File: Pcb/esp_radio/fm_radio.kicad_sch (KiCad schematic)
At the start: 21 parts, among them J3 Antenna, U5 RDA5807FP, Y2 32.768kHz

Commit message: Move custom components to kicad_common_library.
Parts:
- U5: symbol RDA5807FP:RDA5807FP -> kicad_common_lib:RDA5807FP
- renumbered TP10 to TP16, TP12 to TP17, TP11 to TP18
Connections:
- net +12V renamed +10V
- net I2C.SCLK renamed I2C.SCL
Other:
- note added: "Addr: 0b00100000"

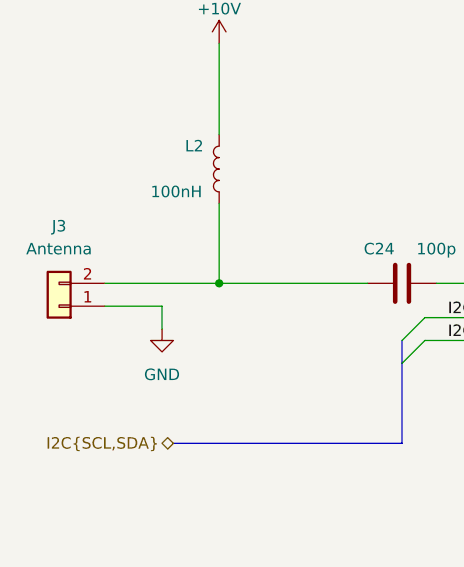
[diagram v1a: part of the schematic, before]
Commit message: Add components layout on PCB
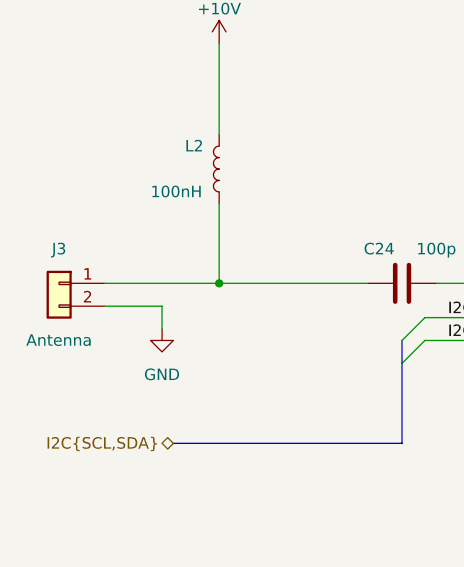
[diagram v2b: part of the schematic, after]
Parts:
- C24: footprint (none) -> kicad_common_lib:C_0805
- J3: footprint (none) -> Connector_JST:JST_XH_S2B-XH-A-1_1x02_P2.50mm_Horizontal
- L1, L2: footprint (none) -> Inductor_SMD:L_1206_3216Metric_Pad1.42x1.75mm_HandSolder
- R6: footprint (none) -> kicad_common_lib:R_0805
- TP16, TP17, TP18: footprint (none) -> TestPoint:TestPoint_THTPad_D2.0mm_Drill1.0mm
- Y2: footprint (none) -> Crystal:Crystal_HC18-U_Vertical
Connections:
- net GND: now also J3.2 (Pin_2); no longer J3.1 (Pin_1)
- net at C24.1, L2.1: now also J3.1 (Pin_1); no longer J3.2 (Pin_2)
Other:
- moved on the sheet: J3

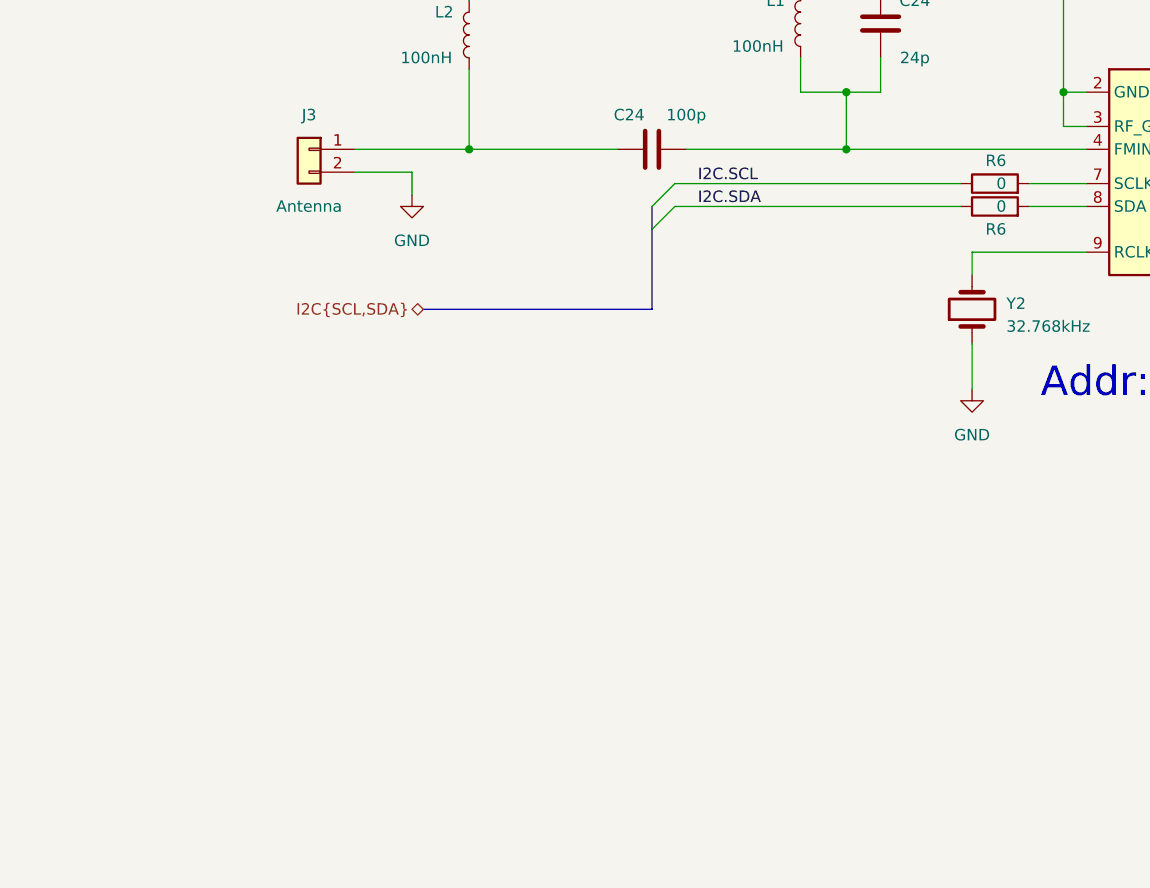
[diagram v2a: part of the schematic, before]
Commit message: Add chip select emulation for i2c devices
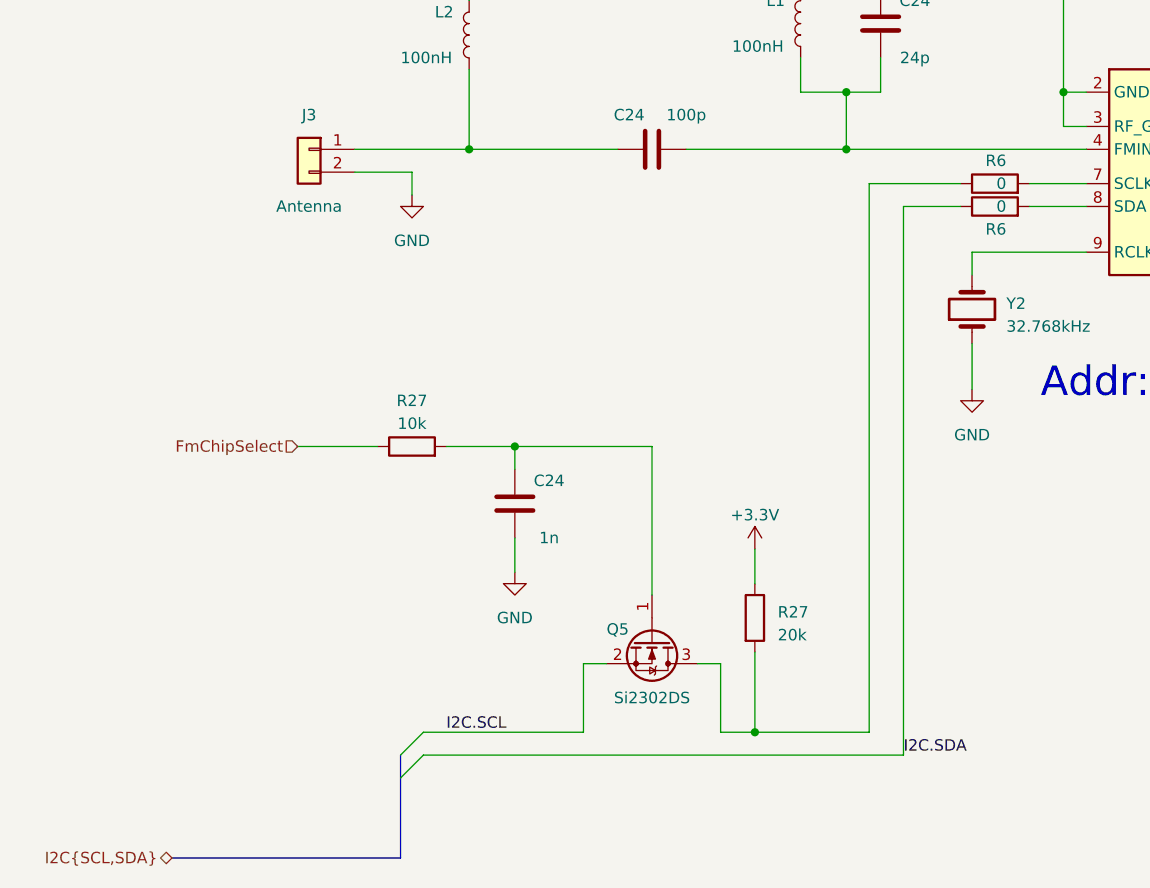
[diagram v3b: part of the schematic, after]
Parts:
- added C24: 1n, kicad_common_lib:C_0805, symbol Device:C
- added Q5: Si2302DS, Package_TO_SOT_SMD:SOT-23, symbol kicad_common_lib:AO3416
- added R27: 20k, kicad_common_lib:R_0805, symbol Device:R
- added R27: 10k, kicad_common_lib:R_0805, symbol Device:R
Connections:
- net +3.3V: now also R27.1
- net GND: now also C24.2
- net I2C.SCL: now also Q5.2 (S); no longer R6.1
- new net: C24.1, Q5.1 (G), R27.2
- new net: Q5.3 (D), R27.2, R6.1
- new net FmChipSelect: R27.1

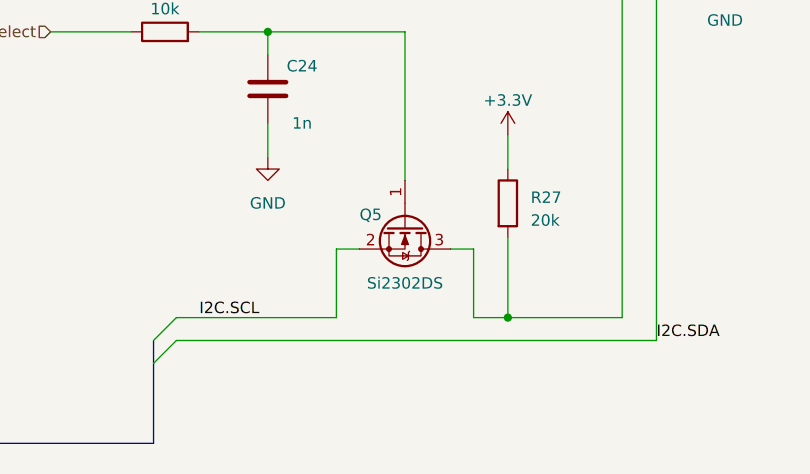
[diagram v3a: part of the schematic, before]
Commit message: Export gerber file.
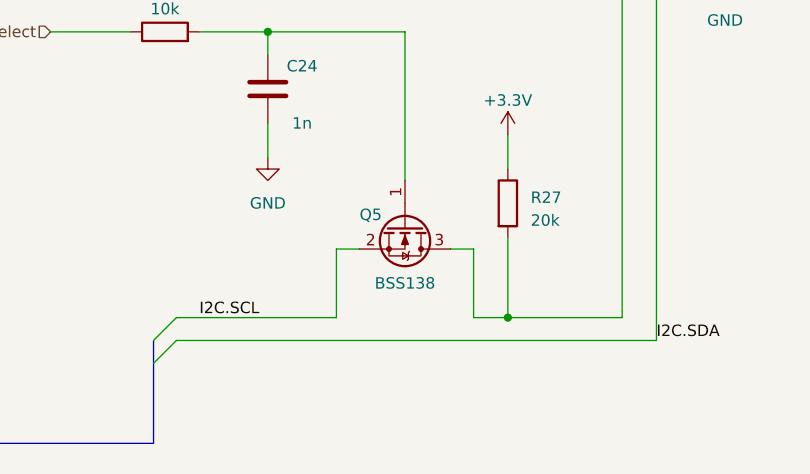
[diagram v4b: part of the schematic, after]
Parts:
- Q5: value Si2302DS -> BSS138
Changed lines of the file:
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@@
       (effects (font (size 1.27 1.27)))
     )
-    (property "Value" "Si2302DS" (at 86.36 152.4 90)
+    (property "Value" "BSS138" (at 86.36 152.4 90)
       (effects (font (size 1.27 1.27)))
     )
